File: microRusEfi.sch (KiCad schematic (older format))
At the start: 37 parts, among them J4 Conn_02x05_Counter_Clockwise, U3 molex_48pin_MRE, U7 XC6206 3.3V

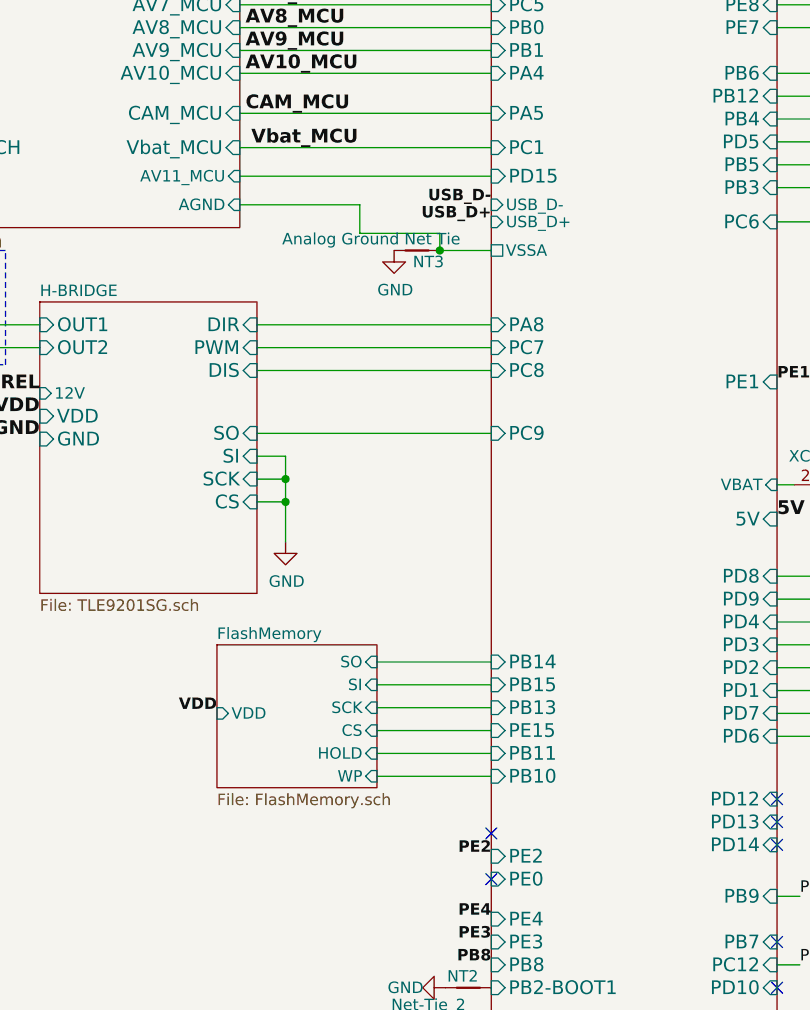
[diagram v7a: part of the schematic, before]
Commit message: Added op-amp pull down on un-used op-amp. https://github.com/rusefi/hw_microRusEfi/issues/127
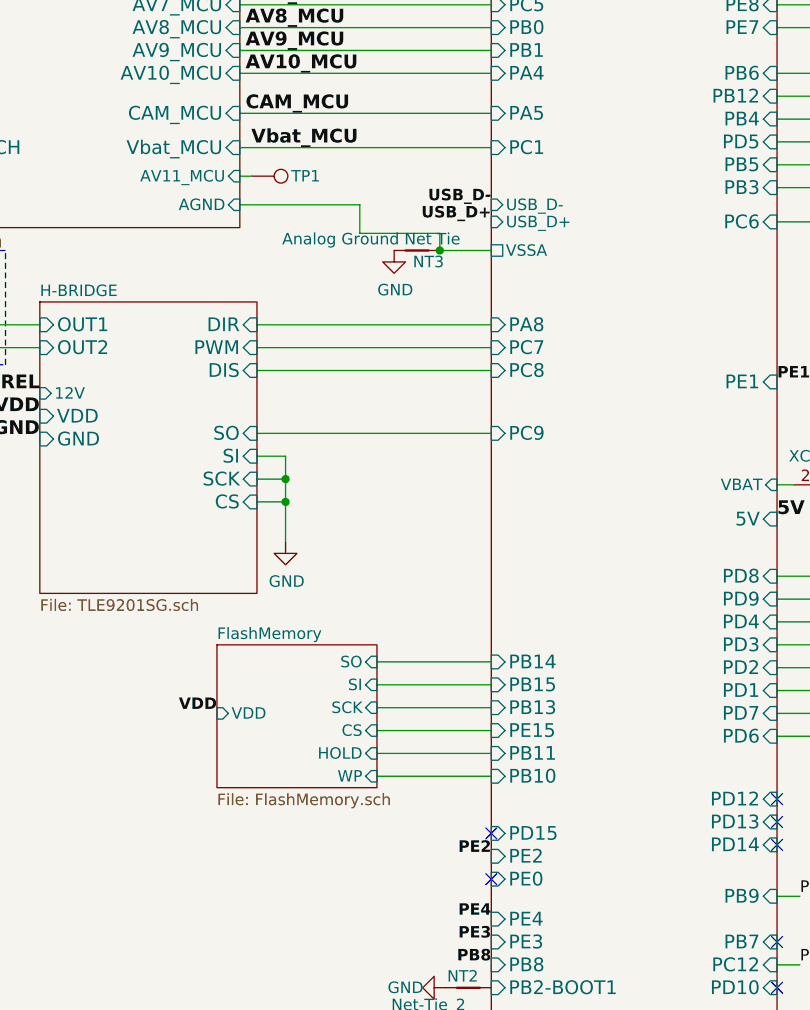
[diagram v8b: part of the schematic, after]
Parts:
- added TP1: TP, TestPoint:TestPoint_Pad_D2.0mm, symbol Connector:TestPoint
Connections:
- net ADC/AV11_MCU: now also TP1.1
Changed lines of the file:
@@
 F20 "PD11" I R 7950 9525 60
 F21 "PD13" I R 7950 8100 60
-F22 "PD15" I L 6700 5275 60
+F22 "PD15" I L 6700 8150 60
 F23 "PC0" I L 6700 3925 60
 F24 "PC2" I L 6700 4225 60
@@
 F77 "PB2-BOOT1" I L 6700 8825 60
 F78 "PA8" I L 6700 5925 60
-F80 "USB_D+" I L 6700 5475 50
-F81 "USB_D-" I L 6700 5400 50
-F82 "VBAT" I R 7950 6625 50
-F83 "VSSA" U L 6700 5600 50
+F79 "USB_D+" I L 6700 5475 50
+F80 "USB_D-" I L 6700 5400 50
+F81 "VBAT" I R 7950 6625 50
+F82 "VSSA" U L 6700 5600 50
 $EndSheet
 Text Label 10050 8175 0    60   ~ 12
@@
 	0    -1   -1   0
 $EndComp
-Wire Wire Line
-	5600 5275 6700 5275
+$Comp
+L Connector:TestPoint TP1
+U 1 1 5EC5BC44
+P 5650 5275
+F 0 "TP1" V 5650 5450 50  0000 L CNN
+F 1 "TP" H 5708 5302 50  0001 L CNN
+F 2 "TestPoint:TestPoint_Pad_D2.0mm" H 5850 5275 50  0001 C CNN
+F 3 "~" H 5850 5275 50  0001 C CNN
+F 4 "DNP" H -500 350 50  0001 C CNN "Part #"
+F 5 "DNP" H -500 350 50  0001 C CNN "VEND"
+F 6 "DNP" H -500 350 50  0001 C CNN "VEND#"
+F 7 "DNP" H -500 350 50  0001 C CNN "Manufacturer"
+	1    5650 5275
+	0    1    1    0
+$EndComp
+Wire Wire Line
+	5600 5275 5650 5275
 $EndSCHEMATC
